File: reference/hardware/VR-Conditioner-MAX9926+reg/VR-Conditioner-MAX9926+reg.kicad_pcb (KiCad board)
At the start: 2 copper layers, 19.1 x 19.7 mm, 24 parts, among them J1 8-pin header, J2 Edge, U1 MAX9926UAEE+, U2 AMS1117CD-5.0

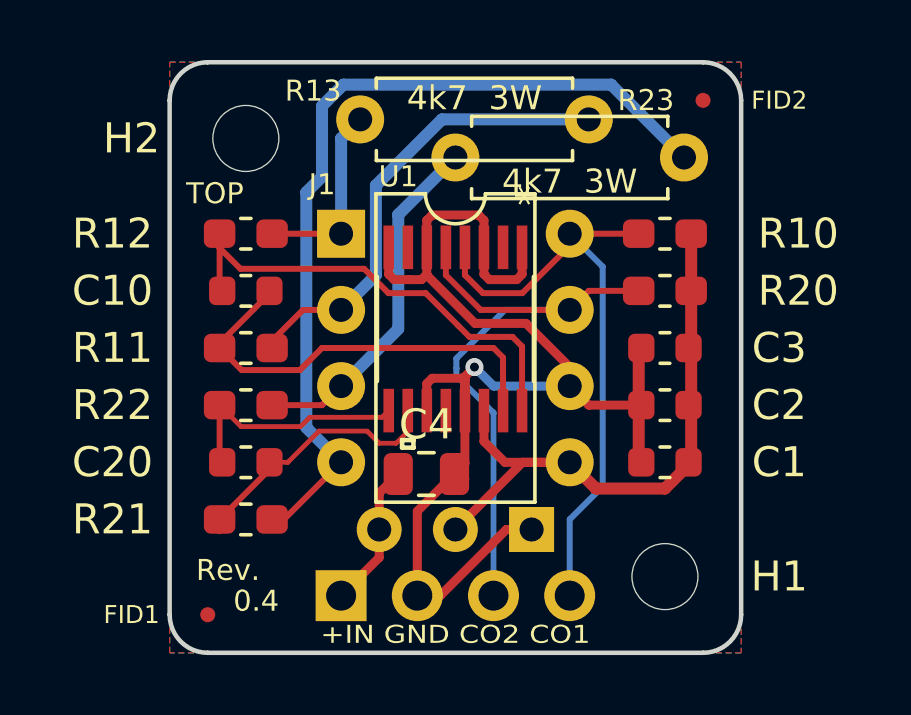
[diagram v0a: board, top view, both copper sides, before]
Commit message: Reroute a trace to avoid 2 traces between a pair of pins.
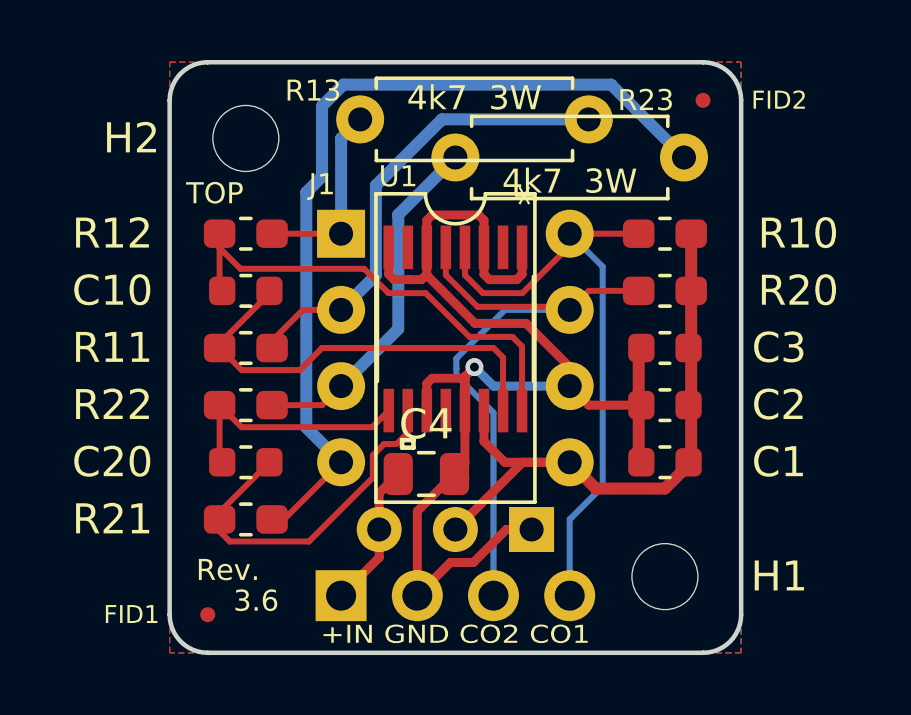
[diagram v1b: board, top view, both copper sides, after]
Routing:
- net Net-(C20-Pad1): track 9.01 -> 12.1 mm
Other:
- board text added: "3.6"
- board text removed: "0.4"
